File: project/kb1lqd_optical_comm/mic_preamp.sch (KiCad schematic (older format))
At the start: 15 parts

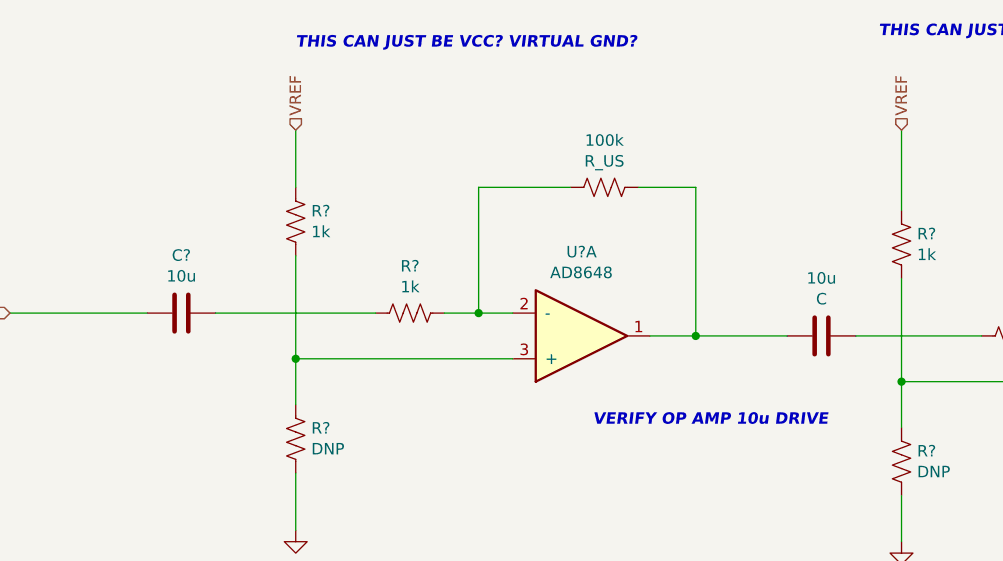
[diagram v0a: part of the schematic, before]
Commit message: Updated with better values and text.
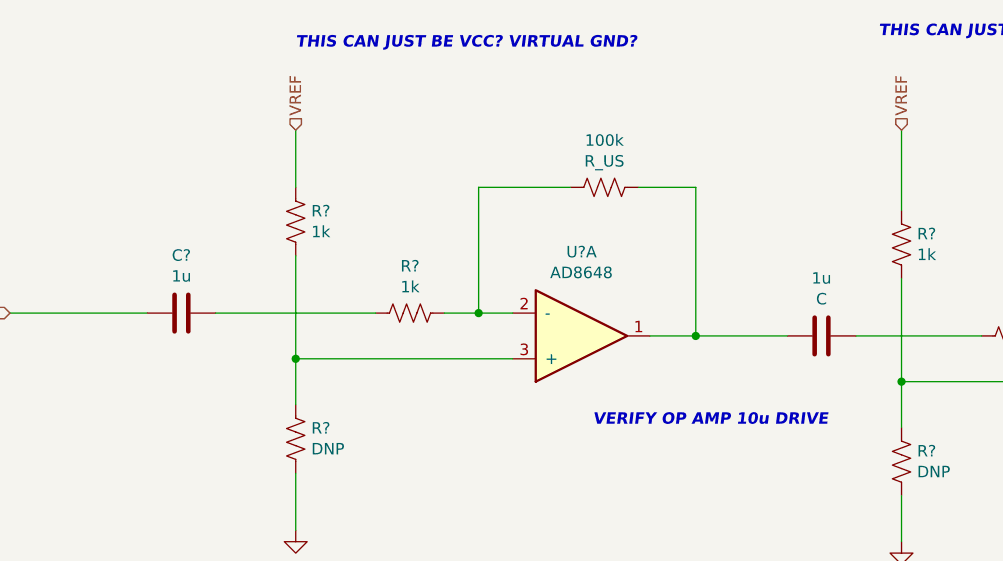
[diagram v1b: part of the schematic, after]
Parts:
- C?: value 10u -> 1u
- renumbered 10u to 1u
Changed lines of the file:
@@
 $Descr A4 11693 8268
 encoding utf-8
-Sheet 2 4
+Sheet 4 4
 Title ""
 Date ""
@@
 P 3000 3700
 F 0 "C?" V 2748 3700 50  0000 C CNN
-F 1 "10u" V 2839 3700 50  0000 C CNN
+F 1 "1u" V 2839 3700 50  0000 C CNN
 F 2 "" H 3038 3550 50  0001 C CNN
 F 3 "~" H 3000 3700 50  0001 C CNN
@@
 $EndComp
 $Comp
-L Device:C 10u
+L Device:C 1u
 U 1 1 5F660E6D
 P 5800 3800
-F 0 "10u" V 5548 3800 50  0000 C CNN
+F 0 "1u" V 5548 3800 50  0000 C CNN
 F 1 "C" V 5639 3800 50  0000 C CNN
 F 2 "" H 5838 3650 50  0001 C CNN

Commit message: Adding updates.
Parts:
- R? (x2): value DNP -> 1k
- R? (x2): value 1k -> 3.24k
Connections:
- net VREF is gone; now on net +5V: R?.2, R?.2
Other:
- note added: "1.2V single supply VREF"
- note added: "AV= 1 to 21 V/V"
- note added: "AV=100V/V"
- note added: "GBP = 2.0 MHz"
- note added: "GBP = 240KHz"
- note removed: "THIS CAN JUST BE VCC? VIRTUAL GND?"
- note removed: "VERIFY OP AMP 10u DRIVE"
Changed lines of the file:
@@
 P 3500 4250
 F 0 "R?" H 3432 4204 50  0000 R CNN
-F 1 "DNP" H 3432 4295 50  0000 R CNN
+F 1 "1k" H 3432 4295 50  0000 R CNN
 F 2 "" V 3540 4240 50  0001 C CNN
 F 3 "~" H 3500 4250 50  0001 C CNN
@@
 P 3500 3300
 F 0 "R?" H 3432 3254 50  0000 R CNN
-F 1 "1k" H 3432 3345 50  0000 R CNN
+F 1 "3.24k" H 3432 3345 50  0000 R CNN
 F 2 "" V 3540 3290 50  0001 C CNN
 F 3 "~" H 3500 3300 50  0001 C CNN
@@
 P 6150 4350
 F 0 "R?" H 6082 4304 50  0000 R CNN
-F 1 "DNP" H 6082 4395 50  0000 R CNN
+F 1 "1k" H 6082 4395 50  0000 R CNN
 F 2 "" V 6190 4340 50  0001 C CNN
 F 3 "~" H 6150 4350 50  0001 C CNN
@@
 P 6150 3400
 F 0 "R?" H 6082 3354 50  0000 R CNN
-F 1 "1k" H 6082 3445 50  0000 R CNN
+F 1 "3.24k" H 6082 3445 50  0000 R CNN
 F 2 "" V 6190 3390 50  0001 C CNN
 F 3 "~" H 6150 3400 50  0001 C CNN
@@
 	1    0    0    -1
 $EndComp
-Text HLabel 6150 2900 1    50   Input ~ 0
-VREF
-Text HLabel 3500 2900 1    50   Input ~ 0
-VREF
-Text Notes 4800 4200 0    50   Italic 10
-VERIFY OP AMP 10u DRIVE
-Text Notes 7150 4350 0    50   Italic 10
-VERIFY OP AMP 10u DRIVE
-Text Notes 3500 2550 0    50   Italic 10
-THIS CAN JUST BE VCC? VIRTUAL GND?
-Text Notes 6050 2500 0    50   Italic 10
-THIS CAN JUST BE VCC? VIRTUAL GND?
+Text Notes 4500 4300 0    50   ~ 0
+AV=100V/V
+Text Notes 7150 4350 0    50   ~ 0
+AV= 1 to 21 V/V
+$Comp
+L power:+5V #PWR?
+U 1 1 5F6DB7F0
+P 3500 2900
+F 0 "#PWR?" H 3500 2750 50  0001 C CNN
+F 1 "+5V" H 3515 3073 50  0000 C CNN
+F 2 "" H 3500 2900 50  0001 C CNN
+F 3 "" H 3500 2900 50  0001 C CNN
+	1    3500 2900
+	1    0    0    -1
+$EndComp
+$Comp
+L power:+5V #PWR?
+U 1 1 5F6DDC2B
+P 6150 2900
+F 0 "#PWR?" H 6150 2750 50  0001 C CNN
+F 1 "+5V" H 6165 3073 50  0000 C CNN
+F 2 "" H 6150 2900 50  0001 C CNN
+F 3 "" H 6150 2900 50  0001 C CNN
+	1    6150 2900
+	1    0    0    -1
+$EndComp
+Text Notes 3550 3850 0    50   ~ 0
+1.2V single supply VREF
+Text Notes 6200 3950 0    50   ~ 0
+1.2V single supply VREF
+Text Notes 4500 4450 0    50   ~ 0
+GBP = 240KHz
+Text Notes 7150 4500 0    50   ~ 0
+GBP = 2.0 MHz
 $EndSCHEMATC

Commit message: Adding updates for 9/21/2020
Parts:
- added C?: DNP, symbol Device:C
- C?: renamed from 1u; value C -> 1u
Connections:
- net at 100k.2, R?.1, U?.2 (-): now also C?.2
- net at 100k.1, C?.2, U?.1: now also C?.1
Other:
- note added: "Optional LPF"
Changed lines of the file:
@@
 $EndComp
 $Comp
-L Device:C 1u
+L Device:C C?
 U 1 1 5F660E6D
 P 5800 3800
-F 0 "1u" V 5548 3800 50  0000 C CNN
-F 1 "C" V 5639 3800 50  0000 C CNN
+F 0 "C?" V 5548 3800 50  0000 C CNN
+F 1 "1u" V 5639 3800 50  0000 C CNN
 F 2 "" H 5838 3650 50  0001 C CNN
 F 3 "~" H 5800 3800 50  0001 C CNN
@@
 Text Notes 7150 4500 0    50   ~ 0
 GBP = 2.0 MHz
+$Comp
+L Device:C C?
+U 1 1 5F708452
+P 4850 2600
+F 0 "C?" V 4598 2600 50  0000 C CNN
+F 1 "DNP" V 4689 2600 50  0000 C CNN
+F 2 "" H 4888 2450 50  0001 C CNN
+F 3 "~" H 4850 2600 50  0001 C CNN
+	1    4850 2600
+	0    1    1    0
+$EndComp
+Wire Wire Line
+	4700 2600 4300 2600
+Wire Wire Line
+	4300 2600 4300 3150
+Connection ~ 4300 3150
+Wire Wire Line
+	5000 2600 5250 2600
+Wire Wire Line
+	5250 2600 5250 3150
+Connection ~ 5250 3150
+Text Notes 4550 2800 0    50   ~ 0
+Optional LPF
 $EndSCHEMATC

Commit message: Schematic essentially done.
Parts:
- added C? (x2): DNP, symbol Device:C
- gave numbers to parts that had none: 13
- renumbered 100k to 100k1
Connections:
- net AUDIO_OUTPUT: now also C?.1
- net GND: now also C?.2
- net at R21.1, R22.2, U2.5 (+): now also C?.1
- net at R23.1, R24.2, U2.6 (-): now also C?.2
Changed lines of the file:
@@
 $Descr A4 11693 8268
 encoding utf-8
-Sheet 4 5
+Sheet 4 6
 Title ""
 Date ""
@@
 $EndDescr
 $Comp
-L Device:R_US R?
+L Device:R_US R20
 U 1 1 5F64F230
 P 4000 3700
-F 0 "R?" V 3795 3700 50  0000 C CNN
+F 0 "R20" V 3795 3700 50  0000 C CNN
 F 1 "1k" V 3886 3700 50  0000 C CNN
 F 2 "" V 4040 3690 50  0001 C CNN
@@
 $EndComp
 $Comp
-L Device:R_US 100k
+L Device:R_US 100k1
 U 1 1 5F64F8BA
 P 4850 3150
-F 0 "100k" V 4645 3150 50  0000 C CNN
+F 0 "100k1" V 4645 3150 50  0000 C CNN
 F 1 "R_US" V 4736 3150 50  0000 C CNN
 F 2 "" V 4890 3140 50  0001 C CNN
@@
 $EndComp
 $Comp
-L kb1lqd_optical_comm:AD8648 U?
+L kb1lqd_optical_comm:AD8648 U2
 U 1 1 5F655125
 P 4100 3400
-F 0 "U?" H 4750 3433 50  0000 C CNN
+F 0 "U2" H 4750 3433 50  0000 C CNN
 F 1 "AD8648" H 4750 3524 50  0000 C CNN
 F 2 "" H 4100 3400 50  0001 C CNN
@@
 $EndComp
 $Comp
-L kb1lqd_optical_comm:AD8648 U?
+L kb1lqd_optical_comm:AD8648 U2
 U 2 1 5F6554DE
 P 6750 3500
-F 0 "U?" H 7400 3533 50  0000 C CNN
+F 0 "U2" H 7400 3533 50  0000 C CNN
 F 1 "AD8648" H 7400 3624 50  0000 C CNN
 F 2 "" H 6750 3500 50  0001 C CNN
@@
 $EndComp
 $Comp
-L kb1lqd_optical_comm:AD8648 U?
+L kb1lqd_optical_comm:AD8648 U2
 U 3 1 5F655A3E
 P 1600 6900
-F 0 "U?" H 2278 7301 50  0000 L CNN
+F 0 "U2" H 2278 7301 50  0000 L CNN
 F 1 "AD8648" H 2278 7210 50  0000 L CNN
 F 2 "" H 1600 6900 50  0001 C CNN
@@
 $EndComp
 $Comp
-L Device:R_US R?
+L Device:R_US R19
 U 1 1 5F65A1AE
 P 3500 4250
-F 0 "R?" H 3432 4204 50  0000 R CNN
+F 0 "R19" H 3432 4204 50  0000 R CNN
 F 1 "1k" H 3432 4295 50  0000 R CNN
 F 2 "" V 3540 4240 50  0001 C CNN
@@
 $EndComp
 $Comp
-L Device:R_US R?
+L Device:R_US R18
 U 1 1 5F65BD96
 P 3500 3300
-F 0 "R?" H 3432 3254 50  0000 R CNN
+F 0 "R18" H 3432 3254 50  0000 R CNN
 F 1 "3.24k" H 3432 3345 50  0000 R CNN
 F 2 "" V 3540 3290 50  0001 C CNN
@@
 	5250 3800 5050 3800
 $Comp
-L Device:C C?
+L Device:C C5
 U 1 1 5F660A05
 P 3000 3700
-F 0 "C?" V 2748 3700 50  0000 C CNN
+F 0 "C5" V 2748 3700 50  0000 C CNN
 F 1 "1u" V 2839 3700 50  0000 C CNN
 F 2 "" H 3038 3550 50  0001 C CNN
@@
 $EndComp
 $Comp
-L Device:C C?
+L Device:C C7
 U 1 1 5F660E6D
 P 5800 3800
-F 0 "C?" V 5548 3800 50  0000 C CNN
+F 0 "C7" V 5548 3800 50  0000 C CNN
 F 1 "1u" V 5639 3800 50  0000 C CNN
 F 2 "" H 5838 3650 50  0001 C CNN
@@
 $EndComp
 $Comp
-L Device:R_US R?
+L Device:R_US R23
 U 1 1 5F666D92
 P 6650 3800
-F 0 "R?" V 6445 3800 50  0000 C CNN
+F 0 "R23" V 6445 3800 50  0000 C CNN
 F 1 "1k" V 6536 3800 50  0000 C CNN
 F 2 "" V 6690 3790 50  0001 C CNN
@@
 $EndComp
 $Comp
-L Device:R_US R?
+L Device:R_US R22
 U 1 1 5F666D9C
 P 6150 4350
-F 0 "R?" H 6082 4304 50  0000 R CNN
+F 0 "R22" H 6082 4304 50  0000 R CNN
 F 1 "1k" H 6082 4395 50  0000 R CNN
 F 2 "" V 6190 4340 50  0001 C CNN
@@
 $EndComp
 $Comp
-L Device:R_US R?
+L Device:R_US R21
 U 1 1 5F666DA6
 P 6150 3400
-F 0 "R?" H 6082 3354 50  0000 R CNN
+F 0 "R21" H 6082 3354 50  0000 R CNN
 F 1 "3.24k" H 6082 3445 50  0000 R CNN
 F 2 "" V 6190 3390 50  0001 C CNN
@@
 	6150 4000 6150 4200
 $Comp
-L Device:R_US R?
+L Device:R_US R24
 U 1 1 5F66D21B
 P 7450 3150
-F 0 "R?" V 7245 3150 50  0000 C CNN
+F 0 "R24" V 7245 3150 50  0000 C CNN
 F 1 "1k" V 7336 3150 50  0000 C CNN
 F 2 "" V 7490 3140 50  0001 C CNN
@@
 Connection ~ 5250 3800
 $Comp
-L Device:R_POT_US RV?
+L Device:R_POT_US RV2
 U 1 1 5F670BBD
 P 7950 3150
-F 0 "RV?" V 7745 3150 50  0000 C CNN
+F 0 "RV2" V 7745 3150 50  0000 C CNN
 F 1 "20k" V 7836 3150 50  0000 C CNN
 F 2 "" H 7950 3150 50  0001 C CNN
@@
 	3150 3700 3850 3700
 $Comp
-L Device:C C?
+L Device:C C4
 U 1 1 5F68FB73
 P 1500 6650
-F 0 "C?" H 1385 6604 50  0000 R CNN
+F 0 "C4" H 1385 6604 50  0000 R CNN
 F 1 "1u" H 1385 6695 50  0000 R CNN
 F 2 "" H 1538 6500 50  0001 C CNN
@@
 $EndComp
 $Comp
-L power:GND #PWR?
+L power:GND #PWR021
 U 1 1 5F690816
 P 1850 6900
-F 0 "#PWR?" H 1850 6650 50  0001 C CNN
+F 0 "#PWR021" H 1850 6650 50  0001 C CNN
 F 1 "GND" H 1855 6727 50  0000 C CNN
 F 2 "" H 1850 6900 50  0001 C CNN
@@
 $EndComp
 $Comp
-L power:+5V #PWR?
+L power:+5V #PWR019
 U 1 1 5F690CB0
 P 1500 6300
-F 0 "#PWR?" H 1500 6150 50  0001 C CNN
+F 0 "#PWR019" H 1500 6150 50  0001 C CNN
 F 1 "+5V" H 1515 6473 50  0000 C CNN
 F 2 "" H 1500 6300 50  0001 C CNN
@@
 	1500 6500 1950 6500
 $Comp
-L power:GND #PWR?
+L power:GND #PWR020
 U 1 1 5F694BA1
 P 1500 6900
-F 0 "#PWR?" H 1500 6650 50  0001 C CNN
+F 0 "#PWR020" H 1500 6650 50  0001 C CNN
 F 1 "GND" H 1505 6727 50  0000 C CNN
 F 2 "" H 1500 6900 50  0001 C CNN
@@
 	3500 4400 3500 4650
 $Comp
-L power:GND #PWR?
+L power:GND #PWR023
 U 1 1 5F69D760
 P 3500 4650
-F 0 "#PWR?" H 3500 4400 50  0001 C CNN
+F 0 "#PWR023" H 3500 4400 50  0001 C CNN
 F 1 "GND" H 3505 4477 50  0000 C CNN
 F 2 "" H 3500 4650 50  0001 C CNN
@@
 $EndComp
 $Comp
-L power:GND #PWR?
+L power:GND #PWR025
 U 1 1 5F69DB42
 P 6150 4700
-F 0 "#PWR?" H 6150 4450 50  0001 C CNN
+F 0 "#PWR025" H 6150 4450 50  0001 C CNN
 F 1 "GND" H 6155 4527 50  0000 C CNN
 F 2 "" H 6150 4700 50  0001 C CNN
@@
 AV= 1 to 21 V/V
 $Comp
-L power:+5V #PWR?
+L power:+5V #PWR022
 U 1 1 5F6DB7F0
 P 3500 2900
-F 0 "#PWR?" H 3500 2750 50  0001 C CNN
+F 0 "#PWR022" H 3500 2750 50  0001 C CNN
 F 1 "+5V" H 3515 3073 50  0000 C CNN
 F 2 "" H 3500 2900 50  0001 C CNN
@@
 $EndComp
 $Comp
-L power:+5V #PWR?
+L power:+5V #PWR024
 U 1 1 5F6DDC2B
 P 6150 2900
-F 0 "#PWR?" H 6150 2750 50  0001 C CNN
+F 0 "#PWR024" H 6150 2750 50  0001 C CNN
 F 1 "+5V" H 6165 3073 50  0000 C CNN
 F 2 "" H 6150 2900 50  0001 C CNN
@@
 GBP = 2.0 MHz
 $Comp
-L Device:C C?
+L Device:C C6
 U 1 1 5F708452
 P 4850 2600
-F 0 "C?" V 4598 2600 50  0000 C CNN
+F 0 "C6" V 4598 2600 50  0000 C CNN
 F 1 "DNP" V 4689 2600 50  0000 C CNN
 F 2 "" H 4888 2450 50  0001 C CNN
@@
 Text Notes 4550 2800 0    50   ~ 0
 Optional LPF
+$Comp
+L Device:C C?
+U 1 1 5FE70959
+P 7650 2550
+F 0 "C?" V 7398 2550 50  0000 C CNN
+F 1 "DNP" V 7489 2550 50  0000 C CNN
+F 2 "" H 7688 2400 50  0001 C CNN
+F 3 "~" H 7650 2550 50  0001 C CNN
+	1    7650 2550
+	0    1    1    0
+$EndComp
+Wire Wire Line
+	7500 2550 7000 2550
+Wire Wire Line
+	7000 2550 7000 3150
+Connection ~ 7000 3150
+Wire Wire Line
+	7800 2550 8450 2550
+Wire Wire Line
+	8450 2550 8450 3150
+Connection ~ 8450 3150
+$Comp
+L Device:C C?
+U 1 1 5FE72A8C
+P 5800 4350
+F 0 "C?" V 5548 4350 50  0000 C CNN
+F 1 "DNP" V 5639 4350 50  0000 C CNN
+F 2 "" H 5838 4200 50  0001 C CNN
+F 3 "~" H 5800 4350 50  0001 C CNN
+	1    5800 4350
+	1    0    0    -1
+$EndComp
+Wire Wire Line
+	5800 4200 5800 4000
+Wire Wire Line
+	5800 4000 6150 4000
+Wire Wire Line
+	5800 4500 5800 4750
+$Comp
+L power:GND #PWR?
+U 1 1 5FE74CD5
+P 5800 4750
+F 0 "#PWR?" H 5800 4500 50  0001 C CNN
+F 1 "GND" H 5805 4577 50  0000 C CNN
+F 2 "" H 5800 4750 50  0001 C CNN
+F 3 "" H 5800 4750 50  0001 C CNN
+	1    5800 4750
+	1    0    0    -1
+$EndComp
 $EndSCHEMATC

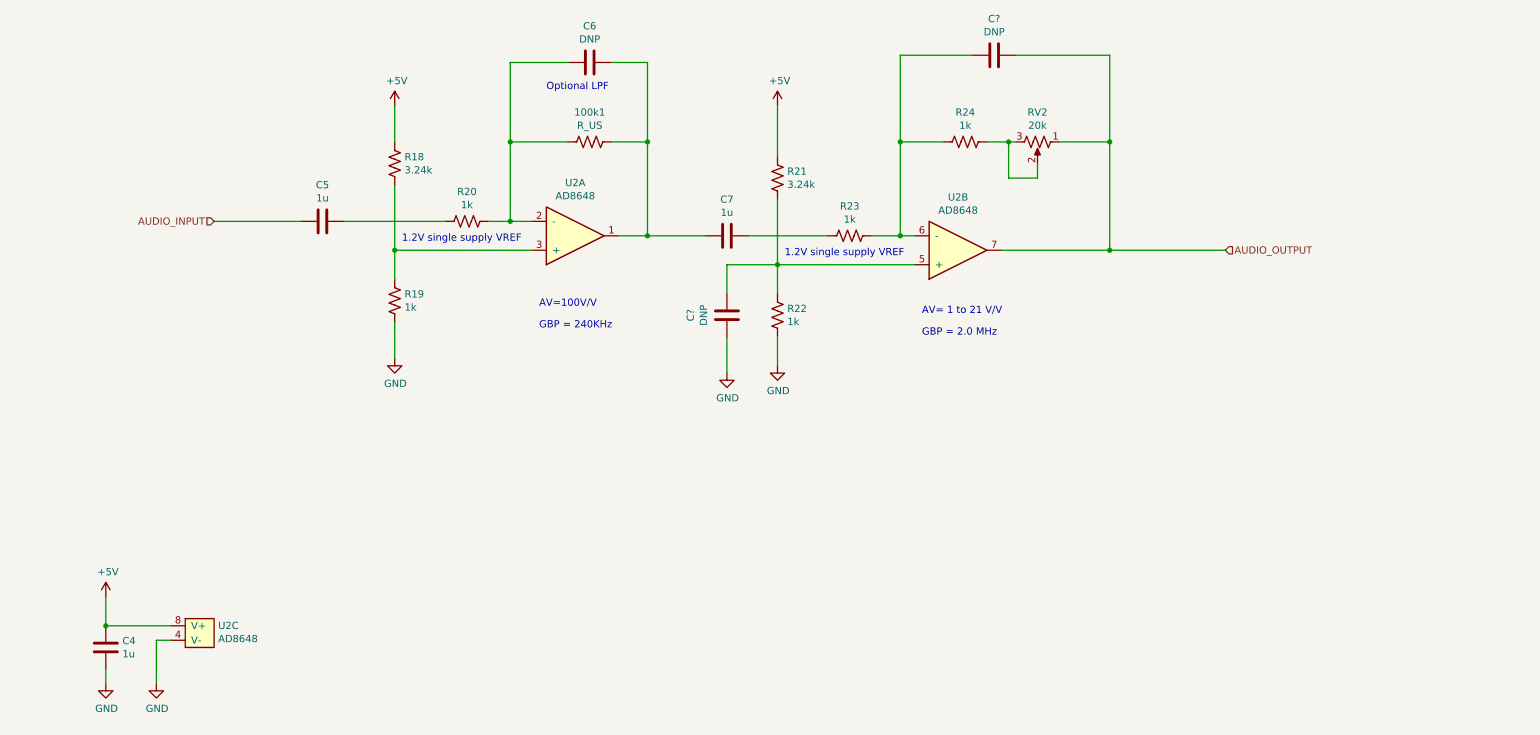
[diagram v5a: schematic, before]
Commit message: Fixing ERC errors.
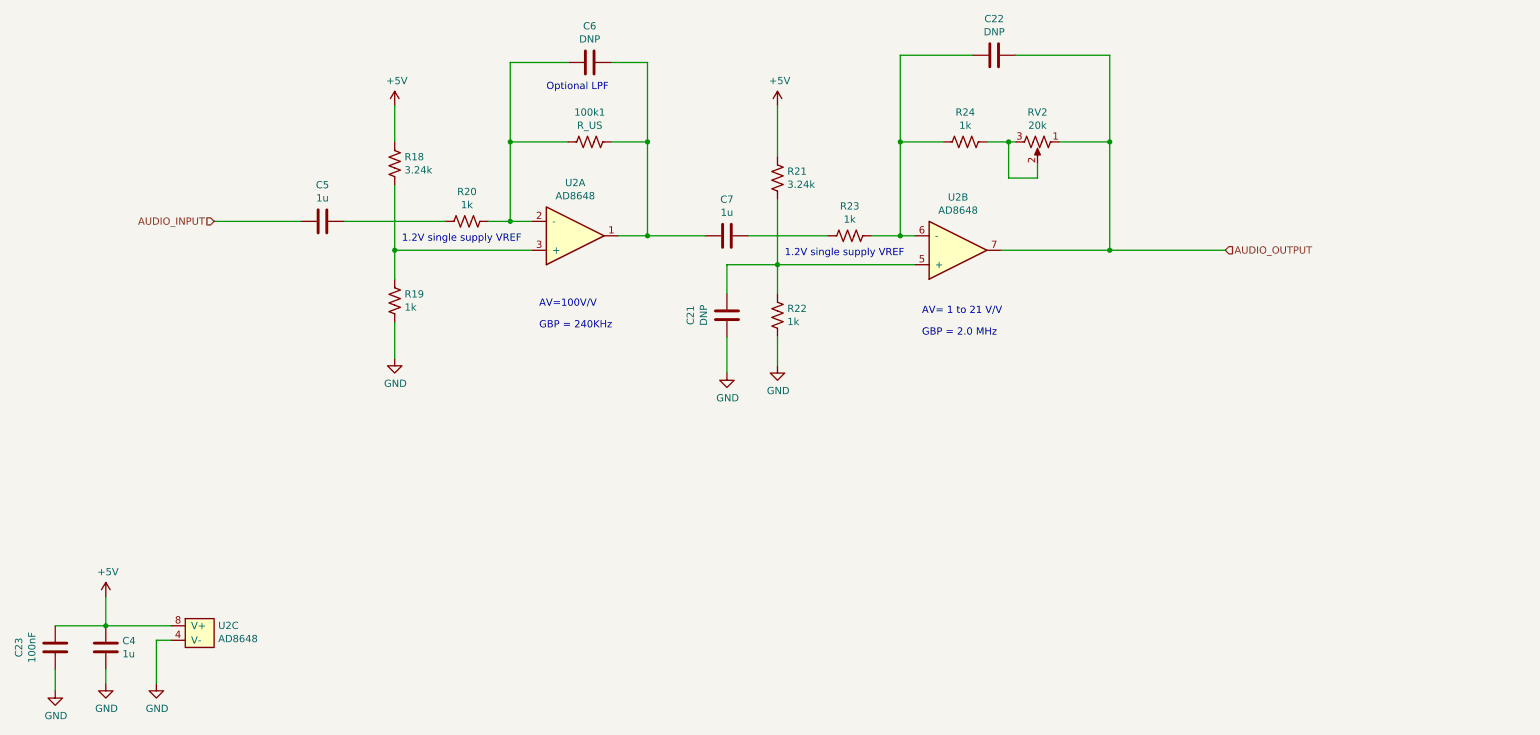
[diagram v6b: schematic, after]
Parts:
- added C23: 100nF, symbol Device:C
- gave numbers to parts that had none: 2
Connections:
- net +5V: now also C23.1
- net GND: now also C23.2
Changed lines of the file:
@@
 Wire Wire Line
 	1850 6600 1850 6900
-Wire Wire Line
-	1500 6500 1950 6500
 $Comp
 L power:GND #PWR020
@@
 Optional LPF
 $Comp
-L Device:C C?
+L Device:C C22
 U 1 1 5FE70959
 P 7650 2550
-F 0 "C?" V 7398 2550 50  0000 C CNN
+F 0 "C22" V 7398 2550 50  0000 C CNN
 F 1 "DNP" V 7489 2550 50  0000 C CNN
 F 2 "" H 7688 2400 50  0001 C CNN
@@
 Connection ~ 8450 3150
 $Comp
-L Device:C C?
+L Device:C C21
 U 1 1 5FE72A8C
 P 5800 4350
-F 0 "C?" V 5548 4350 50  0000 C CNN
+F 0 "C21" V 5548 4350 50  0000 C CNN
 F 1 "DNP" V 5639 4350 50  0000 C CNN
 F 2 "" H 5838 4200 50  0001 C CNN
@@
 	5800 4500 5800 4750
 $Comp
-L power:GND #PWR?
+L power:GND #PWR0104
 U 1 1 5FE74CD5
 P 5800 4750
-F 0 "#PWR?" H 5800 4500 50  0001 C CNN
+F 0 "#PWR0104" H 5800 4500 50  0001 C CNN
 F 1 "GND" H 5805 4577 50  0000 C CNN
 F 2 "" H 5800 4750 50  0001 C CNN
@@
 	1    0    0    -1
 $EndComp
+$Comp
+L Device:C C23
+U 1 1 5FE90BA9
+P 1150 6650
+F 0 "C23" V 898 6650 50  0000 C CNN
+F 1 "100nF" V 989 6650 50  0000 C CNN
+F 2 "" H 1188 6500 50  0001 C CNN
+F 3 "~" H 1150 6650 50  0001 C CNN
+	1    1150 6650
+	1    0    0    -1
+$EndComp
+Wire Wire Line
+	1500 6500 1950 6500
+Wire Wire Line
+	1150 6500 1500 6500
+Wire Wire Line
+	1150 6800 1150 6950
+$Comp
+L power:GND #PWR0107
+U 1 1 5FE9505C
+P 1150 6950
+F 0 "#PWR0107" H 1150 6700 50  0001 C CNN
+F 1 "GND" H 1155 6777 50  0000 C CNN
+F 2 "" H 1150 6950 50  0001 C CNN
+F 3 "" H 1150 6950 50  0001 C CNN
+	1    1150 6950
+	1    0    0    -1
+$EndComp
